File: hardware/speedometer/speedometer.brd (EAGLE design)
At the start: 108.9 x 50.2 mm, 123 parts, among them IC1 PIC32MX274F256DT-I_PT, IC10 24LC024SN, IC11 MAX16054AZT+T, IC12 TPS63001DRCT, IC13 TPS63002DRCT, IC2 CSTCE8M00G55-R0, IC3 BQ27441DRZR-G1A, IC7 BQ24075RGTT, IC8 NRF24L01P-T, IC9 CSTCE16M0V53-R0, J1 10104111-0001LF, J2 BAT, J3 CONUFL001-SMD-T, J4 Right_sens, J5 Right, J6 Left_sens, J7 Left, Q1 BC817, Q2 BC817, Q3 BC817, Q4 BC817

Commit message: Minor stuff
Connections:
- removed net UDB_ID: IC1.41
- net USB_ID: now also IC1.41
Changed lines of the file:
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@@
 <signal name="USB_ID">
 <contactref element="J1" pad="4"/>
-</signal>
-<signal name="UDB_ID">
 <contactref element="IC1" pad="41"/>
+<wire x1="-25.095" y1="-71.097" x2="-28.8875" y2="-87.075" width="0" layer="19" extent="1-1"/>
 </signal>
 <signal name="N$21">

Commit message: Laser ctl logic added
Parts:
- added U1: SN74AHC1G08DBVR, SN74AHC1G08DBVR:SOT95P280X145-5N
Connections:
- removed net LASER_RIGHT_CTL: R38.1
- new net LASER_MOD: IC1.3, U1.1
- new net N$42: R38.1, U1.4
- net +3V3: now also U1.5
- net CTL_R: now also U1.2
- net GND: now also U1.3
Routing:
- net LASER_RIGHT_CTL: track 22.8 -> 0.00 mm
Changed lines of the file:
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@@
 <attribute name="SPICEPREFIX" value="R" x="-41.275" y="-200.025" size="1.778" layer="27" display="off"/>
+</element>
+<element name="U1" library="SN74AHC1G08DBVR" package="SOT95P280X145-5N" value="SN74AHC1G08DBVR" x="-39.37" y="-205.105">
+<attribute name="ARROW_PART_NUMBER" value="SN74AHC1G08DBVR" x="-39.37" y="-205.105" size="1.778" layer="27" display="off"/>
+<attribute name="ARROW_PRICE-STOCK" value="https://www.arrow.com/en/products/sn74ahc1g08dbvr/texas-instruments" x="-39.37" y="-205.105" size="1.778" layer="27" display="off"/>
+<attribute name="DESCRIPTION" value="Texas Instruments SN74AHC1G08DBVR, 2-Input AND Logic Gate, 2  5.5 V, 5-Pin SOT-23" x="-39.37" y="-205.105" size="1.778" layer="27" display="off"/>
+<attribute name="HEIGHT" value="1.45mm" x="-39.37" y="-205.105" size="1.778" layer="27" display="off"/>
+<attribute name="MANUFACTURER_NAME" value="Texas Instruments" x="-39.37" y="-205.105" size="1.778" layer="27" display="off"/>
+<attribute name="MANUFACTURER_PART_NUMBER" value="SN74AHC1G08DBVR" x="-39.37" y="-205.105" size="1.778" layer="27" display="off"/>
+<attribute name="RS_PART_NUMBER" value="1218343" x="-39.37" y="-205.105" size="1.778" layer="27" display="off"/>
+<attribute name="RS_PRICE-STOCK" value="http://uk.rs-online.com/web/p/products/1218343" x="-39.37" y="-205.105" size="1.778" layer="27" display="off"/>
 </element>
 </elements>
@@
 <contactref element="JP2" pad="3"/>
 <contactref element="R14" pad="1"/>
+<contactref element="U1" pad="3"/>
+<wire x1="-42.225" y1="-200.025" x2="-40.62" y2="-206.055" width="0" layer="19" extent="1-1"/>
 <wire x1="-36.195" y1="-189.5475" x2="-42.225" y2="-200.025" width="0" layer="19" extent="1-1"/>
 <wire x1="-38.735" y1="-184.15" x2="-36.195" y2="-189.5475" width="0" layer="19" extent="1-1"/>
@@
 <contactref element="R7" pad="2"/>
 <contactref element="JP3" pad="1"/>
+<contactref element="U1" pad="5"/>
+<wire x1="-41.275" y1="-194.945" x2="-38.12" y2="-204.155" width="0" layer="19" extent="1-1"/>
 <wire x1="-40.325" y1="-165.735" x2="-41.275" y2="-194.945" width="0" layer="19" extent="1-1"/>
 <wire x1="-40.325" y1="-149.86" x2="-40.325" y2="-165.735" width="0" layer="19" extent="1-1"/>
@@
 <vertex x="107.6325" y="24.765"/>
 </polygon>
-</signal>
-<signal name="LASER_RIGHT_CTL">
-<contactref element="R38" pad="1"/>
-<wire x1="40.005" y1="20.32" x2="40.3225" y2="20.0025" width="0.254" layer="1"/>
-<wire x1="39.685" y1="36.515" x2="40.005" y2="36.195" width="0.254" layer="1"/>
-<wire x1="40.005" y1="36.195" x2="40.005" y2="20.32" width="0.254" layer="1"/>
-<wire x1="33.655" y1="36.515" x2="39.685" y2="36.515" width="0.254" layer="1"/>
 </signal>
 <signal name="LASER_LEFT_CTL">
@@
 <signal name="CTL_R">
 <contactref element="IC1" pad="27"/>
+<contactref element="U1" pad="2"/>
+<wire x1="-17.757" y1="-77.635" x2="-40.62" y2="-205.105" width="0" layer="19" extent="1-1"/>
 </signal>
 <signal name="IN_L">
@@
 <wire x1="-42.225" y1="-165.735" x2="-42.76" y2="-171.45" width="0" layer="19" extent="1-1"/>
 </signal>
+<signal name="LASER_MOD">
+<contactref element="IC1" pad="3"/>
+<contactref element="U1" pad="1"/>
+<wire x1="-29.233" y1="-74.435" x2="-40.62" y2="-204.155" width="0" layer="19" extent="1-1"/>
+</signal>
+<signal name="N$42">
+<contactref element="U1" pad="4"/>
+<contactref element="R38" pad="1"/>
+<wire x1="33.655" y1="36.515" x2="-38.12" y2="-206.055" width="0" layer="19" extent="1-1"/>
+</signal>
 </signals>

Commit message: notes added
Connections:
- net VDD: now also IC1.42

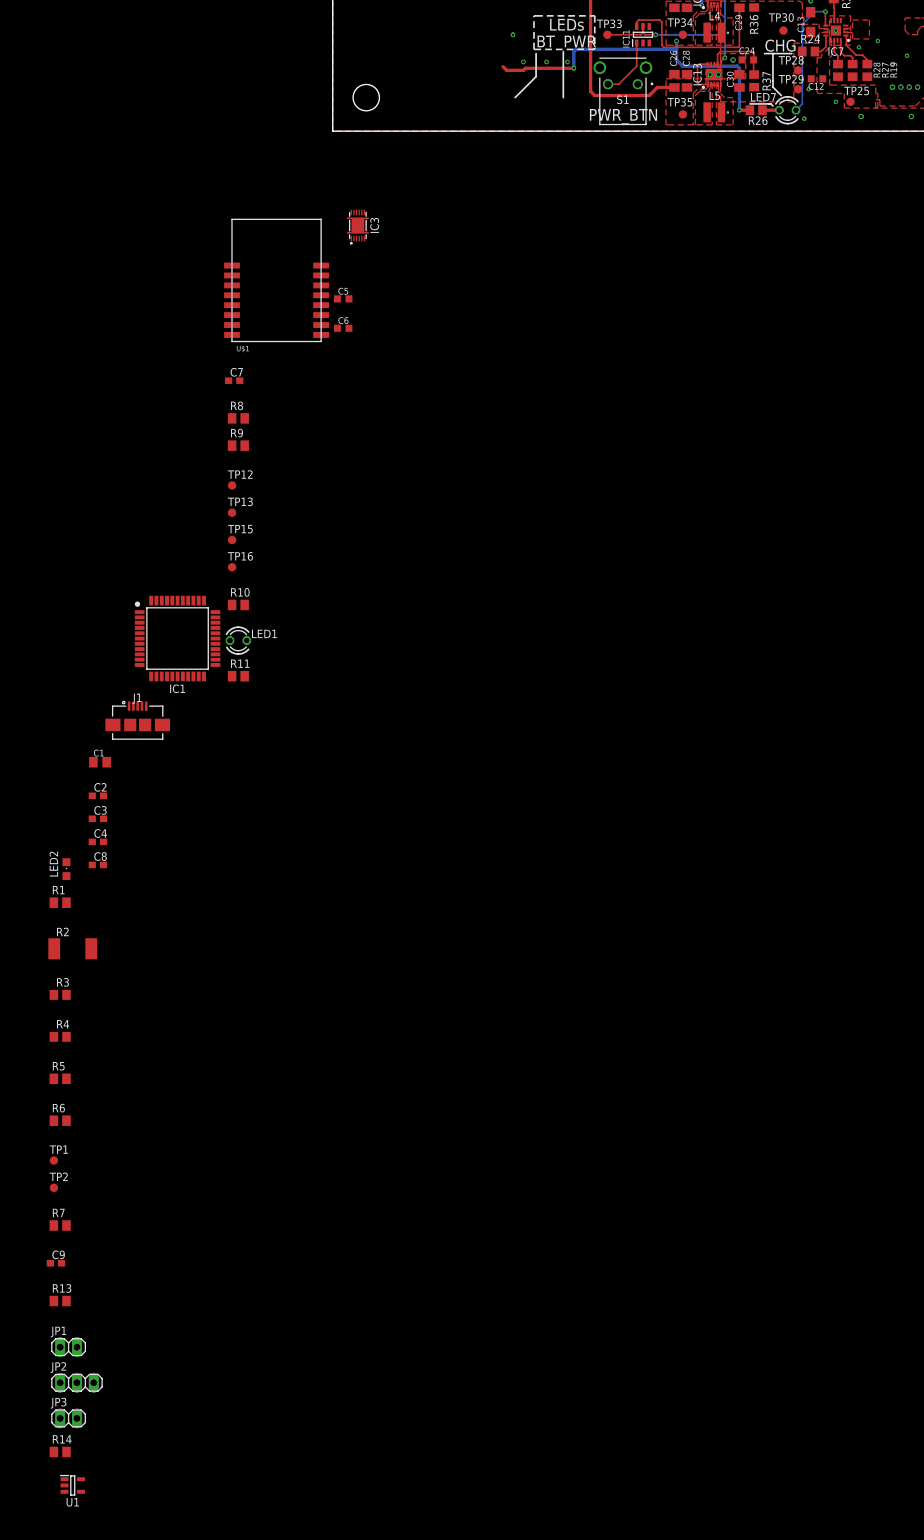
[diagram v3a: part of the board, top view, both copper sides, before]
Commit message: fixed led off while charging the board in off state
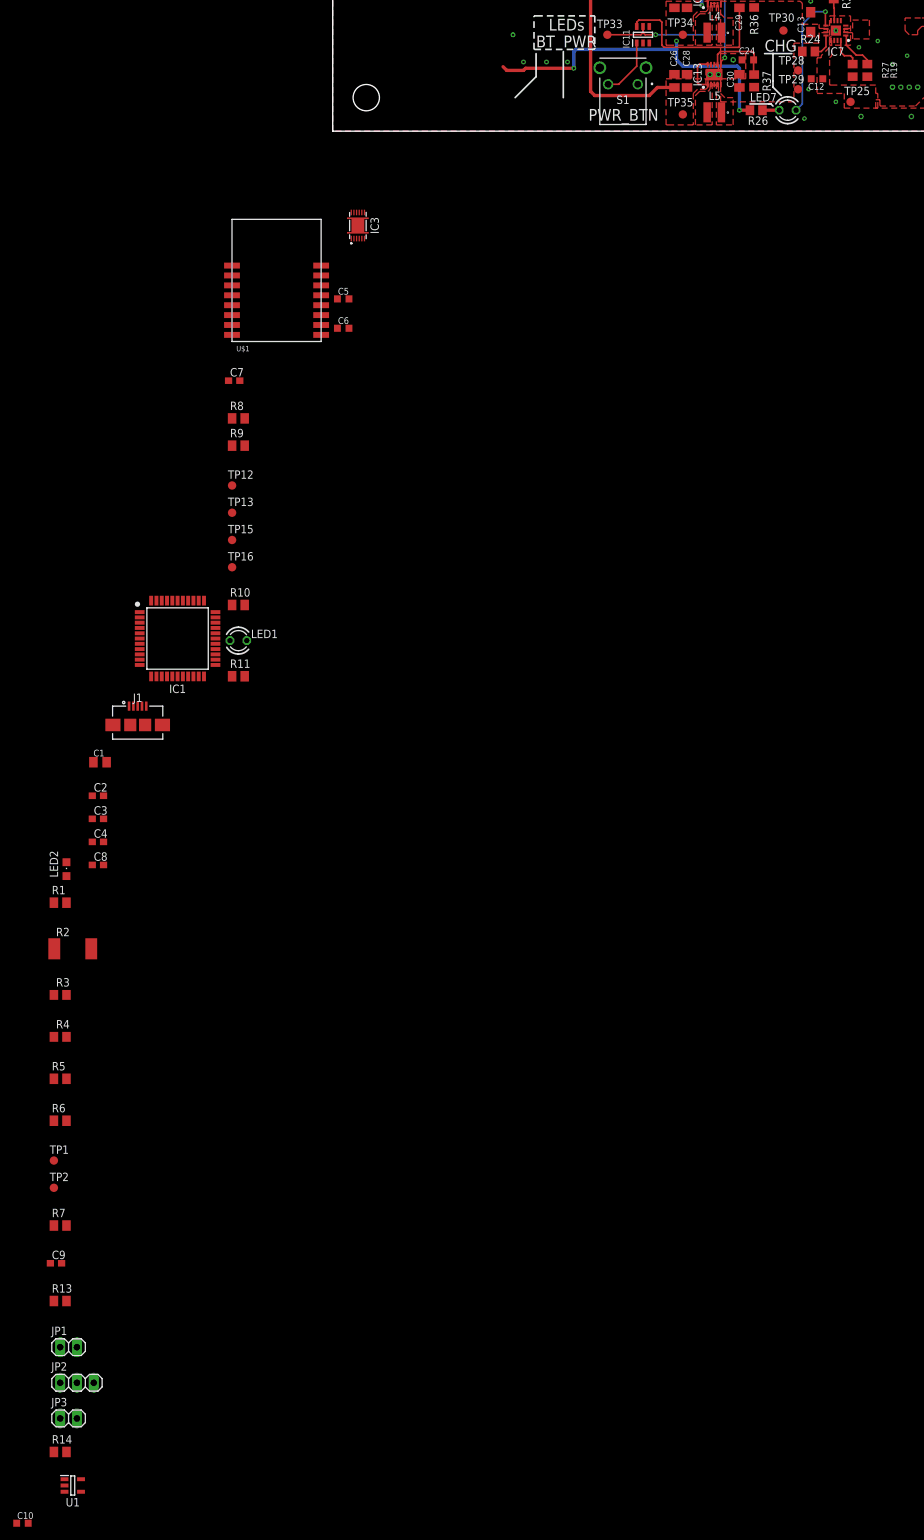
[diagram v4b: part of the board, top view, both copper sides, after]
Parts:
- removed R28: TBD, rcl:R0805
- added C10: 10u, rcl:C0603K
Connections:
- removed net N$14: IC7.14, R28.2
- net +3V3: no longer R26.1
- net GND: now also C10.2; no longer R28.1
- net N$43: now also C10.1
- net VCCINT: now also R26.1
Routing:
- net +3V3: track 286.7 -> 236.5 mm, vias 22 -> 19
- net VCCINT: track 26.1 -> 76.2 mm, vias 0 -> 3
- net N$14: track 3.82 -> 0.00 mm

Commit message: new board dimension
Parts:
- moved C10 294.9 mm to (-35.6, 83.8)
- moved R14 266.8 mm to (-61.0, 66.0)
- moved JP3 266.1 mm to (-45.7, 71.1)
- moved JP2 260.8 mm to (-31.8, 71.1)
- moved JP1 255.3 mm to (-39.4, 71.1)
- moved C9 250.5 mm to (-30.5, 78.7)
- moved TP2 250.3 mm to (-78.7, 87.6)
- moved TP1 245.5 mm to (-73.7, 87.6)
- moved R13 243.6 mm to (-55.9, 66.0)
- moved U1 242.3 mm to (-53.3, 36.8)
- moved R7 239.5 mm to (-15.2, 72.4)
- moved R6 220.6 mm to (-86.4, 66.0)
- moved R5 213.3 mm to (-81.3, 66.0)
- moved R4 203.2 mm to (-45.7, 66.0)
- moved R3 196.9 mm to (-40.6, 66.0)
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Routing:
- net +3V3: track 236.5 -> 0.00 mm, vias 19 -> 0
- net INT_LEFT: track 86.4 -> 0.00 mm, vias 2 -> 0
- net VCCINT: track 76.2 -> 0.00 mm, vias 3 -> 0
- net +5V: track 74.8 -> 0.00 mm, vias 1 -> 0
- net INT_RIGHT: track 68.6 -> 0.00 mm, vias 2 -> 0
- net RIGHT_STS: track 68.3 -> 0.00 mm
- net LEFT_STS: track 55.5 -> 0.00 mm
- net PGED: track 39.6 -> 0.00 mm, vias 1 -> 0
- net PGEC: track 38.3 -> 0.00 mm, vias 1 -> 0
- net SYS_EN: track 34.5 -> 0.00 mm, vias 3 -> 0
- net !MCLR: track 30.7 -> 0.00 mm
- net LASER_LEFT_CTL: track 26.9 -> 0.00 mm, vias 2 -> 0
- net !BAT_CHG: track 20.3 -> 0.00 mm, vias 1 -> 0
- net N$17: track 18.1 -> 0.00 mm
- net N$38: track 17.5 -> 0.00 mm
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- removed copper zone on layer 1, net !APP!/BL
- removed copper zone on layer 1, net +3V3
- removed copper zone on layer 1, net +5V
- removed copper zone on layer 1, net DBG_U2RX
- removed copper zone on layer 1, net DBG_U2TX
- removed copper zone on layer 1, net GND
- removed copper zone on layer 16, net GND
- removed copper zone on layer 1, net N$10
- removed copper zone on layer 16, net N$10
- removed copper zone on layer 1, net N$15
- removed copper zone on layer 1, net N$23
- removed copper zone on layer 1, net N$34
- removed copper zone on layer 1, net N$5
- removed copper zone on layer 1, net N$54
- removed copper zone on layer 1, net N$59
- removed copper zone on layer 1, net N$61
- removed copper zone on layer 1, net VCCINT
- removed copper zone on layer 1, net VDD
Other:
- board size 108.9 x 50.2 mm -> 69.8 x 54.6 mm
- board text removed: "5V - 3V3"
- board text removed: "BT"
- board text removed: "CHG"
- board text removed: "LEDs"
- board text removed: "PWR"
- board text removed: "PWR_BTN"
- board text removed: "RX - TX"
- board text removed: "Speed'o'Meter v0.1-alpha"
- board text removed: "github.com/gabbla/speedometer"
